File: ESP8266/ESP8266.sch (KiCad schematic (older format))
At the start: 47 parts, among them J1 TYPE-C, J2 Micro_SD_Card_Det_Hirose_DM3AT, J3 SirBlue, J4 Conn_01x11, J6 Conn_01x11, Q1 BSS138DW, Q2 MMBT2222A, U1 CP2104, U2 AZ1117-3.3, U3 ESP-12F

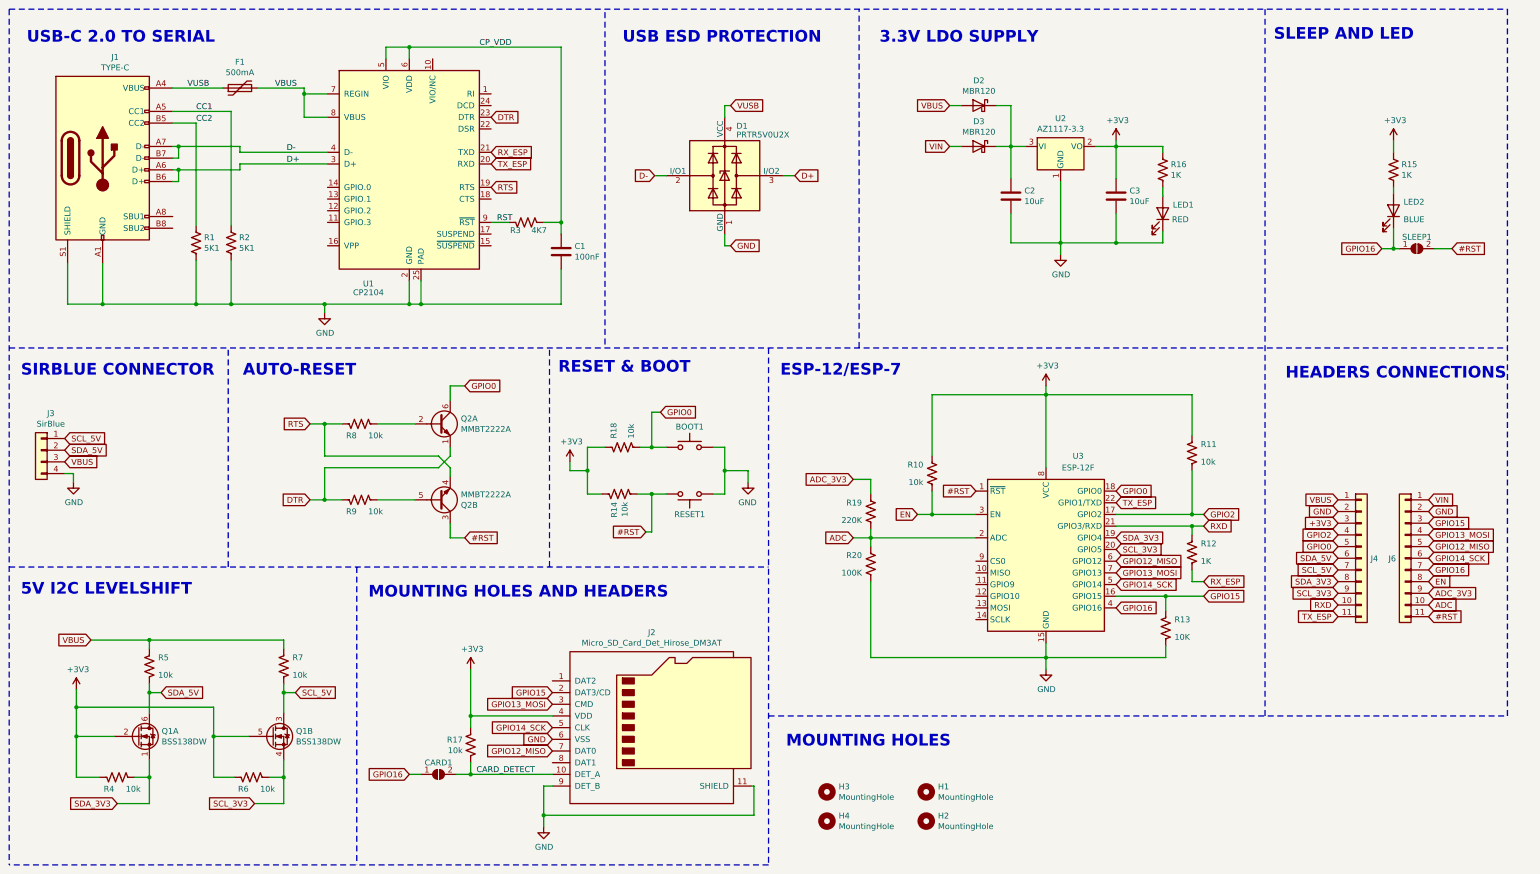
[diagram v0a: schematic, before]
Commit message: ESP8266 V1.3
LED Deletes Added
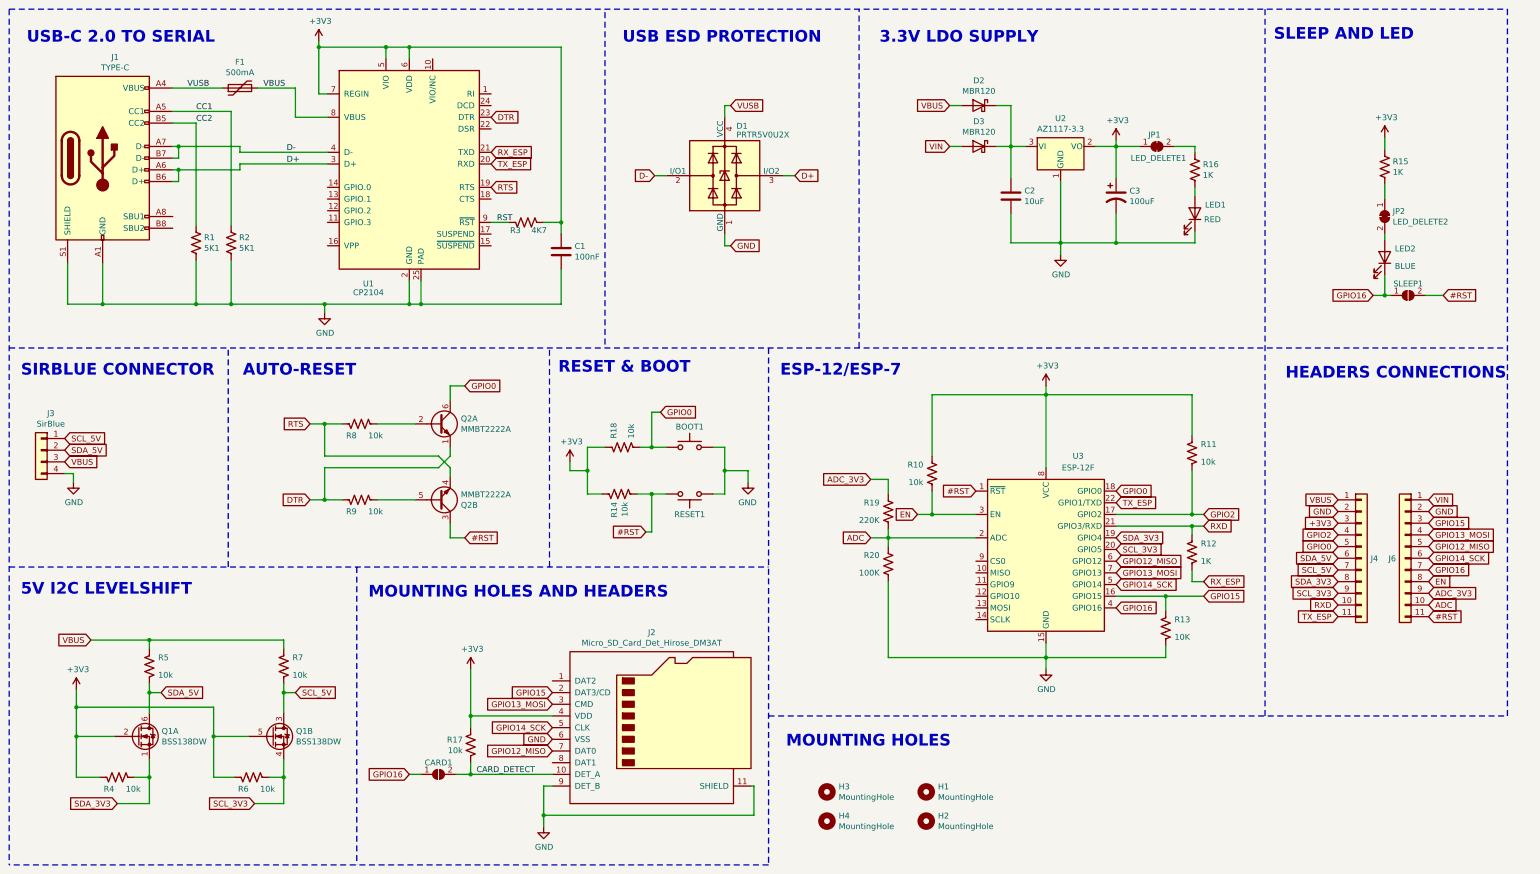
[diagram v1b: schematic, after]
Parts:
- removed C3: 10uF, Capacitor_SMD:C_0805_2012Metric, symbol Device:C
- added C3: 100uF, Capacitor_Tantalum_SMD:CP_EIA-3528-21_Kemet-B, symbol Device:CP1
- added JP1: LED_DELETE1, SirBoardLibrary:SolderJumper-2_P1.3mm_Bridged_RoundedPad1.0x1.5mm, symbol Jumper:SolderJumper_2_Bridged
- added JP2: LED_DELETE2, SirBoardLibrary:SolderJumper-2_P1.3mm_Bridged_RoundedPad1.0x1.5mm, symbol Jumper:SolderJumper_2_Bridged
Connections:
- net CP_VDD is gone; now on net +3V3: C1.1, R3.2, U1.5 (VIO), U1.6 (VDD)
- net +3V3: now also U1.7 (REGIN), C3.1, JP1.1 (A); no longer R16.1
- net GND: now also C3.2
- net VBUS: no longer U1.7 (REGIN)
- net at LED2.2 (A): now also JP2.2 (B); no longer R15.2
- new net: JP2.1 (A), R15.2
- new net: JP1.2 (B), R16.1
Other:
- moved on the sheet: LED1, LED2, R15, R16, R19, R20, SLEEP1
